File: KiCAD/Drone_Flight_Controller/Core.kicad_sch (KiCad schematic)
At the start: 24 parts, among them SW1 SW_Push, SW2 SW_Push, U1 ESP32-S3-MINI-1, U2 TLV75533PDBV, U401 DPS368, U402 BNO055

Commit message: Re-annotate
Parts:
- renumbered C6 to C10, C5 to C11, C1 to C12, C2 to C13, C10 to C2, C4 to C3, C401 to C4, C9 to C5, C3 to C6, C402 to C7, C7 to C8, C8 to C9, R5 to R10, R6 to R11, R2 to R12, R401 to R7, R7 to R8, R3 to R9, U402 to U5, U1 to U6, U401 to U7, U2 to U8

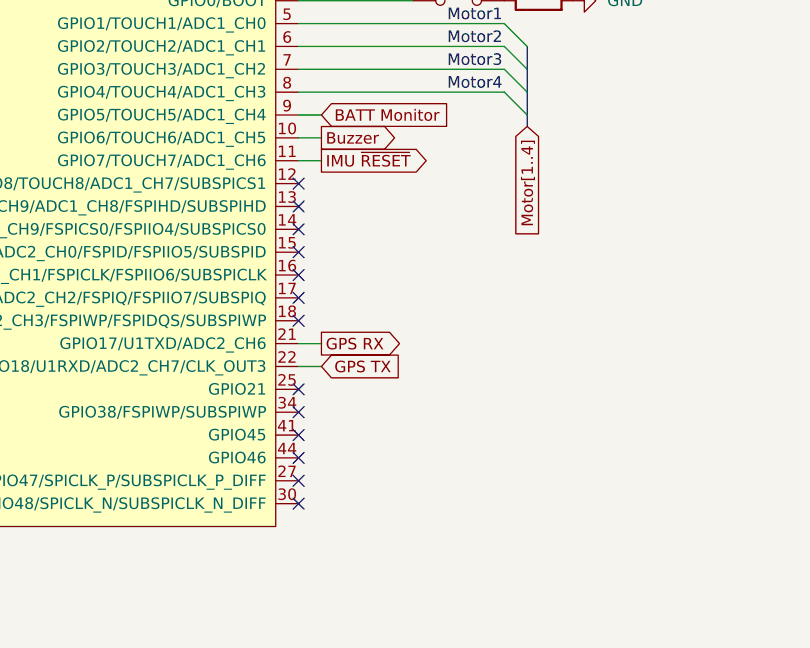
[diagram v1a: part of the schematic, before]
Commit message: Add Status LEDs
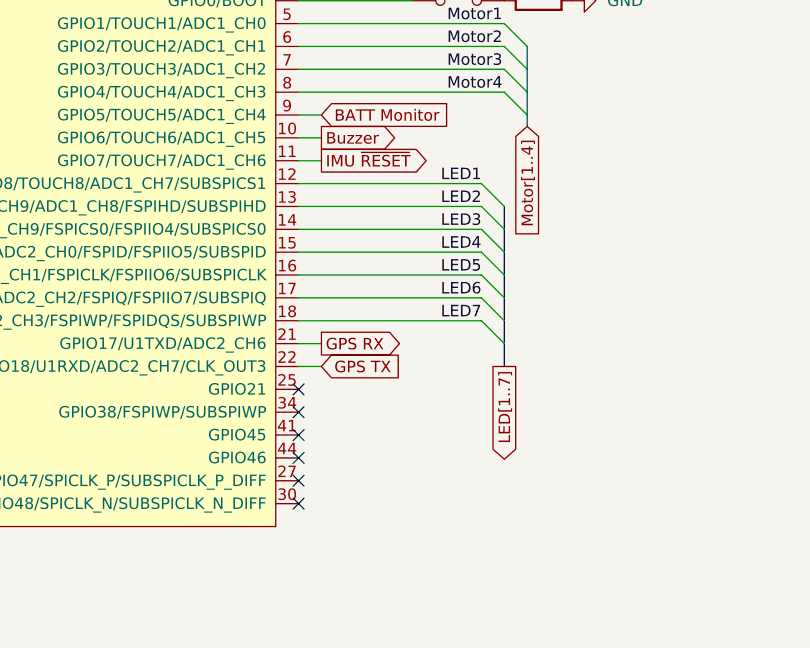
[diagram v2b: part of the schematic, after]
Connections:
- net LED1: now reaches U6.12 (GPIO8/TOUCH8/ADC1_CH7/SUBSPICS1)
- net LED2: now reaches U6.13 (GPIO9/TOUCH9/ADC1_CH8/FSPIHD/SUBSPIHD)
- net LED3: now reaches U6.14 (GPIO10/TOUCH10/ADC1_CH9/FSPICS0/FSPIIO4/SUBSPICS0)
- net LED4: now reaches U6.15 (GPIO11/TOUCH11/ADC2_CH0/FSPID/FSPIIO5/SUBSPID)
- net LED5: now reaches U6.16 (GPIO12/TOUCH12/ADC2_CH1/FSPICLK/FSPIIO6/SUBSPICLK)
- net LED6: now reaches U6.17 (GPIO13/TOUCH13/ADC2_CH2/FSPIQ/FSPIIO7/SUBSPIQ)
- net LED7: now reaches U6.18 (GPIO14/TOUCH14/ADC2_CH3/FSPIWP/FSPIDQS/SUBSPIWP)
- no-connect marks 25 -> 18

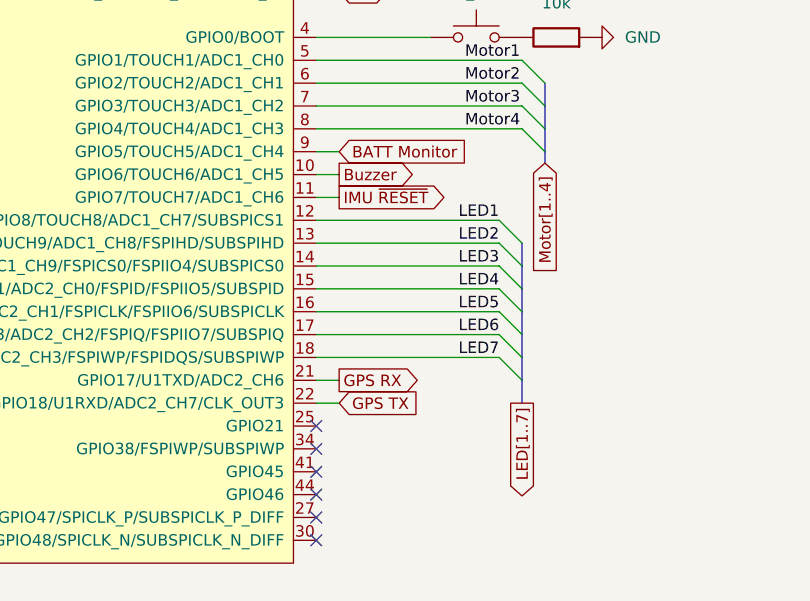
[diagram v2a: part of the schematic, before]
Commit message: Add Current and ESC sense
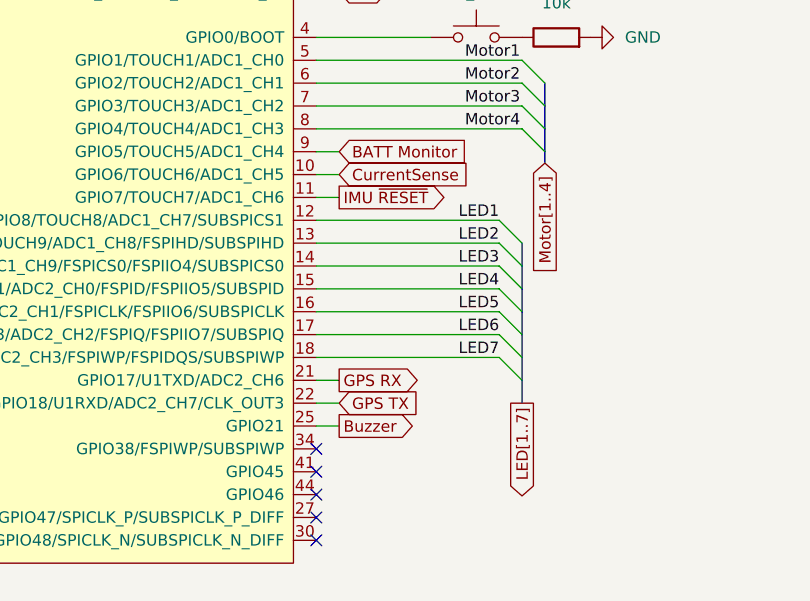
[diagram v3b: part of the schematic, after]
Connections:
- net Buzzer: now also U6.25 (GPIO21); no longer U6.10 (GPIO6/TOUCH6/ADC1_CH5)
- new net CurrentSense: U6.10 (GPIO6/TOUCH6/ADC1_CH5)
- no-connect marks 18 -> 17
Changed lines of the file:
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@@
-	)
-	(no_connect
-		(at 133.35 166.37)
 	)
 	(no_connect
@@
 	(wire
 		(pts
+			(xy 133.35 166.37) (xy 135.89 166.37)
+		)
+		(stroke
+			(width 0)
+			(type default)
+		)
+	)
+	(wire
+		(pts
 			(xy 133.35 156.21) (xy 153.67 156.21)
 		)
@@
 			)
 			(justify left bottom)
+		)
+	)
+	(global_label "Buzzer"
+		(shape output)
+		(at 135.89 166.37 0)
+		(fields_autoplaced yes)
+		(effects
+			(font
+				(size 1.27 1.27)
+			)
+			(justify left)
+		)
+		(property "Intersheetrefs" "${INTERSHEET_REFS}"
+			(at 145.2252 166.37 0)
+			(effects
+				(font
+					(size 1.27 1.27)
+				)
+				(justify left)
+				(hide yes)
+			)
 		)
 	)
@@
 		)
 	)
+	(global_label "CurrentSense"
+		(shape input)
+		(at 135.89 138.43 0)
+		(fields_autoplaced yes)
+		(effects
+			(font
+				(size 1.27 1.27)
+			)
+			(justify left)
+		)
+		(property "Intersheetrefs" "${INTERSHEET_REFS}"
+			(at 151.3937 138.43 0)
+			(effects
+				(font
+					(size 1.27 1.27)
+				)
+				(justify left)
+				(hide yes)
+			)
+		)
+	)
 	(global_label "SCK"
 		(shape output)
@@
 			(effects
 				(font
-					(size 1.27 1.27)
-				)
-				(justify left)
-				(hide yes)
-			)
-		)
-	)
-	(global_label "Buzzer"
-		(shape output)
-		(at 135.89 138.43 0)
-		(fields_autoplaced yes)
-		(effects
-			(font
-				(size 1.27 1.27)
-			)
-			(justify left)
-		)
-		(property "Intersheetrefs" "${INTERSHEET_REFS}"
-			(at 145.2252 138.43 0)
-			(effects
-				(font

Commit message: Add Footprints.
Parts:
- C10: footprint (none) -> Capacitor_SMD:C_0805_2012Metric
- R10, R11, R12, R8, R9: footprint (none) -> Resistor_SMD:R_0805_2012Metric_Pad1.20x1.40mm_HandSolder
- SW1, SW2: footprint (none) -> Button_Switch_SMD:SW_Push_1P1T_NO_CK_KSC6xxJ
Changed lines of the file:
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@@
 			)
 		)
-		(property "Footprint" ""
+		(property "Footprint" "Resistor_SMD:R_0805_2012Metric_Pad1.20x1.40mm_HandSolder"
 			(at 187.96 55.118 90)
 			(effects
@@
 			)
 		)
-		(property "Footprint" ""
+		(property "Footprint" "Button_Switch_SMD:SW_Push_1P1T_NO_CK_KSC6xxJ"
 			(at 151.13 118.11 0)
 			(effects
@@
 			)
 		)
-		(property "Footprint" ""
+		(property "Footprint" "Resistor_SMD:R_0805_2012Metric_Pad1.20x1.40mm_HandSolder"
 			(at 196.342 101.6 90)
 			(effects
@@
 			)
 		)
-		(property "Footprint" ""
+		(property "Footprint" "Capacitor_SMD:C_0805_2012Metric"
 			(at 195.2752 63.5 0)
 			(effects
@@
 			)
 		)
-		(property "Footprint" ""
+		(property "Footprint" "Resistor_SMD:R_0805_2012Metric_Pad1.20x1.40mm_HandSolder"
 			(at 177.292 59.69 90)
 			(effects
@@
 			)
 		)
-		(property "Footprint" ""
+		(property "Footprint" "Resistor_SMD:R_0805_2012Metric_Pad1.20x1.40mm_HandSolder"
 			(at 177.292 46.99 90)
 			(effects
@@
 			)
 		)
-		(property "Footprint" ""
+		(property "Footprint" "Resistor_SMD:R_0805_2012Metric_Pad1.20x1.40mm_HandSolder"
 			(at 160.02 124.968 90)
 			(effects
@@
 			)
 		)
-		(property "Footprint" ""
+		(property "Footprint" "Button_Switch_SMD:SW_Push_1P1T_NO_CK_KSC6xxJ"
 			(at 190.5 102.87 0)
 			(effects

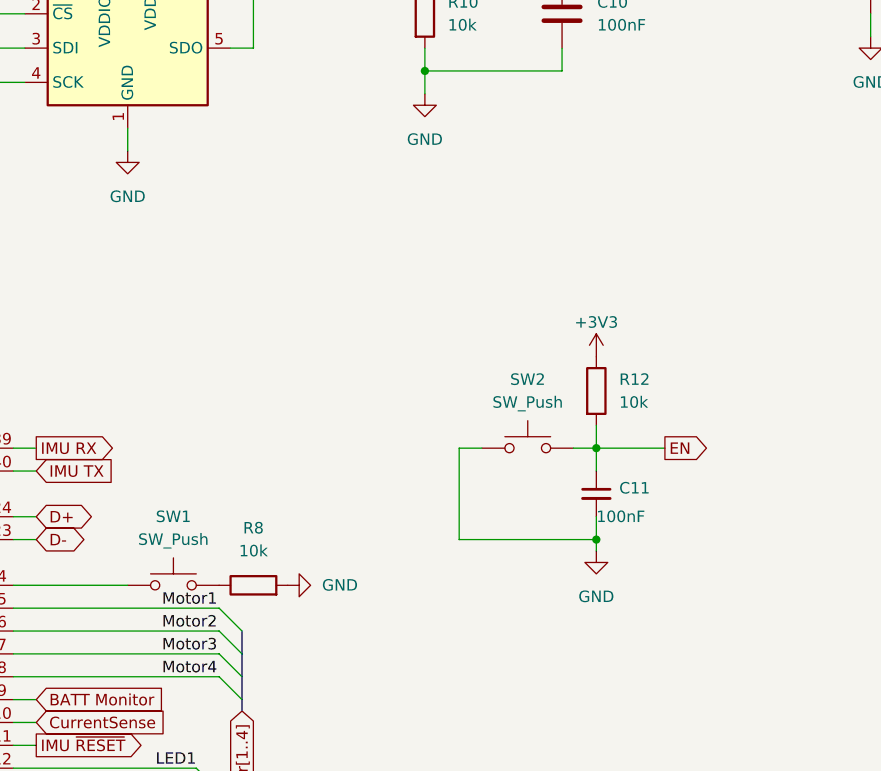
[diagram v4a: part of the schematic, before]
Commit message: Implement feedback from Prof. Parzer
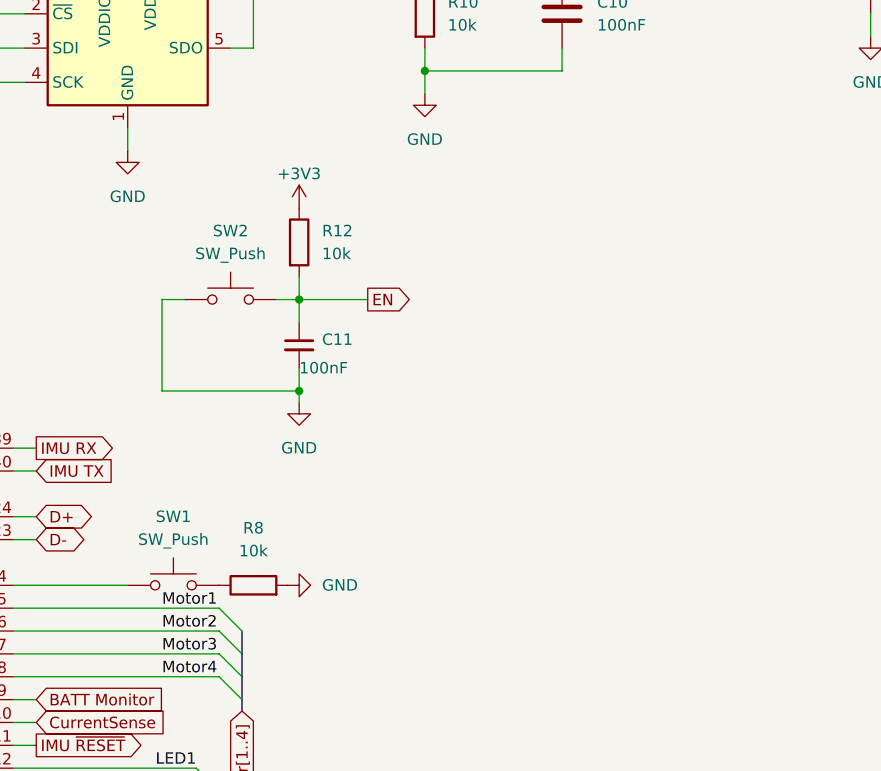
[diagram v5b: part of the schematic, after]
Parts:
- SW1, SW2: footprint Button_Switch_SMD:SW_Push_1P1T_NO_CK_KSC6xxJ -> htl_smd:SW_Push_5.1mm_H1.5mm
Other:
- moved on the sheet: C11, R12, SW2
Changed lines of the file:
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@@
 	(title_block
 		(title "DFC: Peripherals")
-		(date "2025-11-12")
+		(date "2025-11-26")
 		(rev "V3")
 		(company "HTL-Steyr")
@@
 	)
 	(junction
-		(at 198.12 107.95)
+		(at 165.1 91.44)
 		(diameter 0)
 		(color 0 0 0 0)
@@
 	)
 	(junction
-		(at 198.12 118.11)
+		(at 165.1 101.6)
 		(diameter 0)
 		(color 0 0 0 0)
@@
 	(wire
 		(pts
-			(xy 198.12 110.49) (xy 198.12 107.95)
+			(xy 165.1 93.98) (xy 165.1 91.44)
 		)
 		(stroke
@@
 	(wire
 		(pts
-			(xy 198.12 115.57) (xy 198.12 118.11)
+			(xy 165.1 99.06) (xy 165.1 101.6)
 		)
 		(stroke
@@
 	(wire
 		(pts
-			(xy 198.12 105.41) (xy 198.12 107.95)
+			(xy 165.1 88.9) (xy 165.1 91.44)
 		)
 		(stroke
@@
 	(wire
 		(pts
-			(xy 182.88 118.11) (xy 198.12 118.11)
+			(xy 149.86 101.6) (xy 165.1 101.6)
 		)
 		(stroke
@@
 	(wire
 		(pts
-			(xy 182.88 107.95) (xy 182.88 118.11)
+			(xy 149.86 91.44) (xy 149.86 101.6)
 		)
 		(stroke
@@
 	(wire
 		(pts
-			(xy 198.12 107.95) (xy 205.74 107.95)
+			(xy 165.1 91.44) (xy 172.72 91.44)
 		)
 		(stroke
@@
 	(wire
 		(pts
-			(xy 185.42 107.95) (xy 182.88 107.95)
+			(xy 152.4 91.44) (xy 149.86 91.44)
 		)
 		(stroke
@@
 	(wire
 		(pts
-			(xy 195.58 107.95) (xy 198.12 107.95)
+			(xy 162.56 91.44) (xy 165.1 91.44)
 		)
 		(stroke
@@
 	(wire
 		(pts
-			(xy 198.12 118.11) (xy 198.12 119.38)
+			(xy 165.1 101.6) (xy 165.1 102.87)
 		)
 		(stroke
@@
 	(global_label "EN"
 		(shape output)
-		(at 205.74 107.95 0)
+		(at 172.72 91.44 0)
 		(fields_autoplaced yes)
 		(effects
@@
 		)
 		(property "Intersheetrefs" "${INTERSHEET_REFS}"
-			(at 211.1253 107.95 0)
+			(at 178.1053 91.44 0)
 			(effects
 				(font
@@
 	(symbol
 		(lib_id "power:+3V3")
-		(at 198.12 97.79 0)
+		(at 165.1 81.28 0)
 		(unit 1)
 		(exclude_from_sim no)
@@
 		(dnp no)
 		(property "Reference" "#PWR052"
-			(at 198.12 101.6 0)
+			(at 165.1 85.09 0)
 			(effects
 				(font
@@
 		)
 		(property "Value" "+3V3"
-			(at 198.12 93.98 0)
+			(at 165.1 77.47 0)
 			(effects
 				(font
@@
 		)
 		(property "Footprint" ""
-			(at 198.12 97.79 0)
+			(at 165.1 81.28 0)
 			(effects
 				(font
@@
 		)
 		(property "Datasheet" ""
-			(at 198.12 97.79 0)
+			(at 165.1 81.28 0)
 			(effects
 				(font
@@
 		)
 		(property "Description" "Power symbol creates a global label with name \"+3V3\""
-			(at 198.12 97.79 0)
+			(at 165.1 81.28 0)
 			(effects
 				(font
@@
 		(at 87.63 143.51 0)
 		(unit 1)
-		(exclude_from_sim yes)
+		(exclude_from_sim no)
 		(in_bom yes)
 		(on_board yes)
@@
 			)
 		)
-		(property "Footprint" "Button_Switch_SMD:SW_Push_1P1T_NO_CK_KSC6xxJ"
+		(property "Footprint" "htl_smd:SW_Push_5.1mm_H1.5mm"
 			(at 151.13 118.11 0)
 			(effects
@@
 	(symbol
 		(lib_id "Device:R")
-		(at 198.12 101.6 0)
+		(at 165.1 85.09 0)
 		(unit 1)
 		(exclude_from_sim no)
@@
 		(fields_autoplaced yes)
 		(property "Reference" "R12"
-			(at 200.66 100.3299 0)
+			(at 167.64 83.8199 0)
 			(effects
 				(font
@@
 		)
 		(property "Value" "10k"
-			(at 200.66 102.8699 0)
+			(at 167.64 86.3599 0)
 			(effects
 				(font
@@
 		)
 		(property "Footprint" "Resistor_SMD:R_0805_2012Metric_Pad1.20x1.40mm_HandSolder"
-			(at 196.342 101.6 90)
+			(at 163.322 85.09 90)
 			(effects
 				(font
@@
 		)
 		(property "Datasheet" "~"
-			(at 198.12 101.6 0)
+			(at 165.1 85.09 0)
 			(effects
 				(font
@@
 		)
 		(property "Description" "Resistor"
-			(at 198.12 101.6 0)
+			(at 165.1 85.09 0)
 			(effects
 				(font
@@
 	(symbol
 		(lib_id "Device:C_Small")
-		(at 198.12 113.03 0)
+		(at 165.1 96.52 0)
 		(unit 1)
 		(exclude_from_sim no)
@@
 		(dnp no)
 		(property "Reference" "C11"
-			(at 200.66 112.4013 0)
+			(at 167.64 95.8913 0)
 			(effects
 				(font
@@
 		)
 		(property "Value" "100nF"
-			(at 198.12 115.57 0)
+			(at 165.1 99.06 0)
 			(effects
 				(font
@@
 		)
 		(property "Footprint" "Capacitor_SMD:C_0805_2012Metric"
-			(at 198.12 113.03 0)
+			(at 165.1 96.52 0)
 			(effects
 				(font
@@
 		)
 		(property "Datasheet" "~"
-			(at 198.12 113.03 0)
+			(at 165.1 96.52 0)
 			(effects
 				(font
@@
 		)
 		(property "Description" "Unpolarized capacitor, small symbol"
-			(at 198.12 113.03 0)
+			(at 165.1 96.52 0)
 			(effects
 				(font
@@
 	(symbol
 		(lib_id "power:GND")
-		(at 198.12 119.38 0)
+		(at 165.1 102.87 0)
 		(unit 1)
 		(exclude_from_sim no)
@@
 		(fields_autoplaced yes)
 		(property "Reference" "#PWR053"
-			(at 198.12 125.73 0)
+			(at 165.1 109.22 0)
 			(effects
 				(font
@@
 		)
 		(property "Value" "GND"
-			(at 198.12 124.46 0)
+			(at 165.1 107.95 0)
 			(effects
 				(font
@@
 		)
 		(property "Footprint" ""
-			(at 198.12 119.38 0)
+			(at 165.1 102.87 0)
 			(effects
 				(font
@@
 		)
 		(property "Datasheet" ""
-			(at 198.12 119.38 0)
+			(at 165.1 102.87 0)
 			(effects
 				(font
@@
 		)
 		(property "Description" "Power symbol creates a global label with name \"GND\" , ground"
-			(at 198.12 119.38 0)
+			(at 165.1 102.87 0)
 			(effects
 				(font
@@
 		(at 241.3 52.07 0)
 		(unit 1)
-		(exclude_from_sim yes)
+		(exclude_from_sim no)
 		(in_bom yes)
 		(on_board yes)
@@
 	(symbol
 		(lib_id "Switch:SW_Push")
-		(at 190.5 107.95 0)
+		(at 157.48 91.44 0)
 		(unit 1)
 		(exclude_from_sim no)
@@
 		(fields_autoplaced yes)
 		(property "Reference" "SW2"
-			(at 190.5 100.33 0)
+			(at 157.48 83.82 0)
 			(effects
 				(font
@@
 		)
 		(property "Value" "SW_Push"
-			(at 190.5 102.87 0)
+			(at 157.48 86.36 0)
 			(effects
 				(font
@@
 			)
 		)
-		(property "Footprint" "Button_Switch_SMD:SW_Push_1P1T_NO_CK_KSC6xxJ"
-			(at 190.5 102.87 0)
+		(property "Footprint" "htl_smd:SW_Push_5.1mm_H1.5mm"
+			(at 157.48 86.36 0)
 			(effects
 				(font
@@
 		)
 		(property "Datasheet" "~"
-			(at 190.5 102.87 0)
+			(at 157.48 86.36 0)
 			(effects
 				(font
@@
 		)
 		(property "Description" "Push button switch, generic, two pins"
-			(at 190.5 107.95 0)
+			(at 157.48 91.44 0)
 			(effects
 				(font
